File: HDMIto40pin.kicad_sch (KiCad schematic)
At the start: 56 parts, among them J17 TTL 40Pin, J18 I2C EDID, U11 LM1117DT-3.3, U12 FAN5333BSX, U13 TFP401APZPR, U14 24LC02BT-E/LT

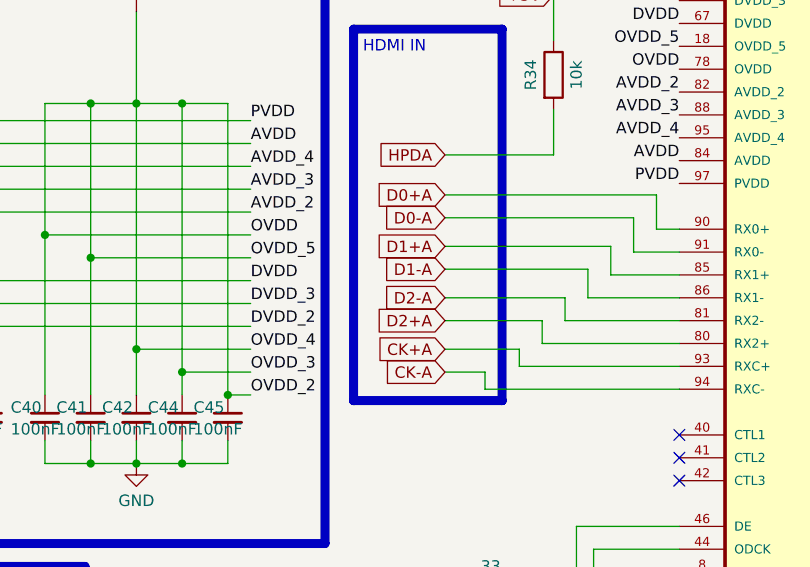
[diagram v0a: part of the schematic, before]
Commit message: fix hdmi traces and push button kill pin supply
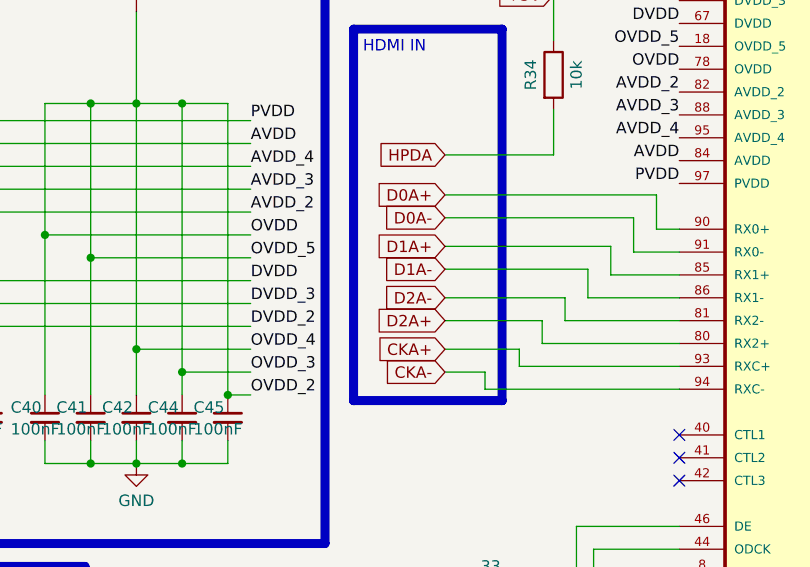
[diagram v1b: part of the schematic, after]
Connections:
- net CK+A renamed CKA+
- net CK-A renamed CKA-
- net D0+A renamed D0A+
- net D0-A renamed D0A-
- net D1+A renamed D1A+
- net D1-A renamed D1A-
- net D2+A renamed D2A+
- net D2-A renamed D2A-

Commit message: update layout pcb & zip tesi
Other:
- moved on the sheet: FB11

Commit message: aggiunto pin enable switch per schermo composito
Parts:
- RN1, RN2, RN3, RN4, RN5, RN6, RN7: footprint Resistor_SMD:R_Array_Convex_4x0603 -> EXB28V330JX:EXB28V_PAN
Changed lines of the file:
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@@
 			)
 		)
-		(property "Footprint" "Resistor_SMD:R_Array_Convex_4x0603"
+		(property "Footprint" "EXB28V330JX:EXB28V_PAN"
 			(at 213.995 74.93 90)
 			(effects
@@
 			)
 		)
-		(property "Footprint" "Resistor_SMD:R_Array_Convex_4x0603"
+		(property "Footprint" "EXB28V330JX:EXB28V_PAN"
 			(at 213.995 44.45 90)
 			(effects
@@
 			)
 		)
-		(property "Footprint" "Resistor_SMD:R_Array_Convex_4x0603"
+		(property "Footprint" "EXB28V330JX:EXB28V_PAN"
 			(at 123.825 103.505 90)
 			(effects
@@
 			)
 		)
-		(property "Footprint" "Resistor_SMD:R_Array_Convex_4x0603"
+		(property "Footprint" "EXB28V330JX:EXB28V_PAN"
 			(at 213.995 64.77 90)
 			(effects
@@
 			)
 		)
-		(property "Footprint" "Resistor_SMD:R_Array_Convex_4x0603"
+		(property "Footprint" "EXB28V330JX:EXB28V_PAN"
 			(at 213.995 54.61 90)
 			(effects
@@
 			)
 		)
-		(property "Footprint" "Resistor_SMD:R_Array_Convex_4x0603"
+		(property "Footprint" "EXB28V330JX:EXB28V_PAN"
 			(at 213.995 95.25 90)
 			(effects
@@
 			)
 		)
-		(property "Footprint" "Resistor_SMD:R_Array_Convex_4x0603"
+		(property "Footprint" "EXB28V330JX:EXB28V_PAN"
 			(at 213.995 85.09 90)
 			(effects

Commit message: update zip
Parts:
- removed D3: BAT54, Package_TO_SOT_SMD:TSOT-23_HandSoldering, symbol Device:D_Schottky
- removed U12: FAN5333BSX, FAN5333:SOT-23-5_ONS, symbol FAN5333:FAN5333BSX
- added C46: 100nF, Capacitor_SMD:C_0603_1608Metric_Pad1.08x0.95mm_HandSolder, symbol Device:C
- added C47: 10uF, Capacitor_SMD:C_0603_1608Metric_Pad1.08x0.95mm_HandSolder, symbol Device:C
- added D7: SS14, Diode_SMD:D_SMA, symbol Diode:SS14
- added FB13: BLM31KN471SZ1L, Inductor_SMD:L_1206_3216Metric_Pad1.22x1.90mm_HandSolder, symbol Device:FerriteBead
- added R47: 910k, Resistor_SMD:R_0603_1608Metric_Pad0.98x0.95mm_HandSolder, symbol Device:R
- added R48: 30k, Resistor_SMD:R_0603_1608Metric_Pad0.98x0.95mm_HandSolder, symbol Device:R
- added U16: PAM2841SR, PAM2841:PAM2841, symbol PAM2841:PAM2841SR
- C35: value 10uF -> 1uF
- D2: value D_Zener -> MM3Z24VST1G
- J17: footprint Connector_FFC-FPC:TE_4-1734839-0_1x40-1MP_P0.5mm_Horizontal -> Connector_FFC-FPC:Omron_XF2M-4015-1A_1x40-1MP_P0.5mm_Horizontal
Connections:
- net +24V: now also D7.1 (K)
- net +5V: now also D4.2 (A), L4.1, C47.1, U16.2 (VIN); no longer L4.2
- net GND: now also C46.2, FB13.2, R48.1, U16.5 (GND); no longer C26.2, C27.2, C38.2
- net LEDK: now also U16.6 (FB)
- net at R37.2: now also U16.3 (ENA); no longer D4.2 (A)
- new net: C46.1, U16.4 (COMP)
- new net: R47.1, R48.2, U16.7 (OVP)
- new net: D7.2 (A), L4.2, R47.2, U16.8 (SW)
- new net BKLGNDPWR: C26.2, C27.2, C38.2, C47.2, FB13.1, U16.1 (PGND)
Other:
- moved on the sheet: C26, C27, C35, C38, D2, D4, JP2, JP3, L4, R36, R37, R38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
